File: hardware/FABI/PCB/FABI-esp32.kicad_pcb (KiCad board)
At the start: 2 copper layers, 41 x 73 mm, 93 parts, among them J1 PJ320D, J10 Conn_01x06, J11 PJ320D, J12 Conn_01x08, J13 tp, J14 tp, J15 tp, J16 tp, J17 tp, J2 PJ320D, J3 PJ320D, J4 PJ320D, J5 PJ320D, J6 PJ320D, J7 PJ320D, J8 Conn_01x04, J9 USB_OTG, Q1 BC847, Q2 BSH108, Q3 BC847, Q4 BSH108, Q5 BSH108, Q6 BSH108, SW1 SW_Push, U1 ESP32-WROOM, U3 LPC11U14FBD, U4 TSR 1 (0.5) -2433, Y1 JA-12.000-18-DFE

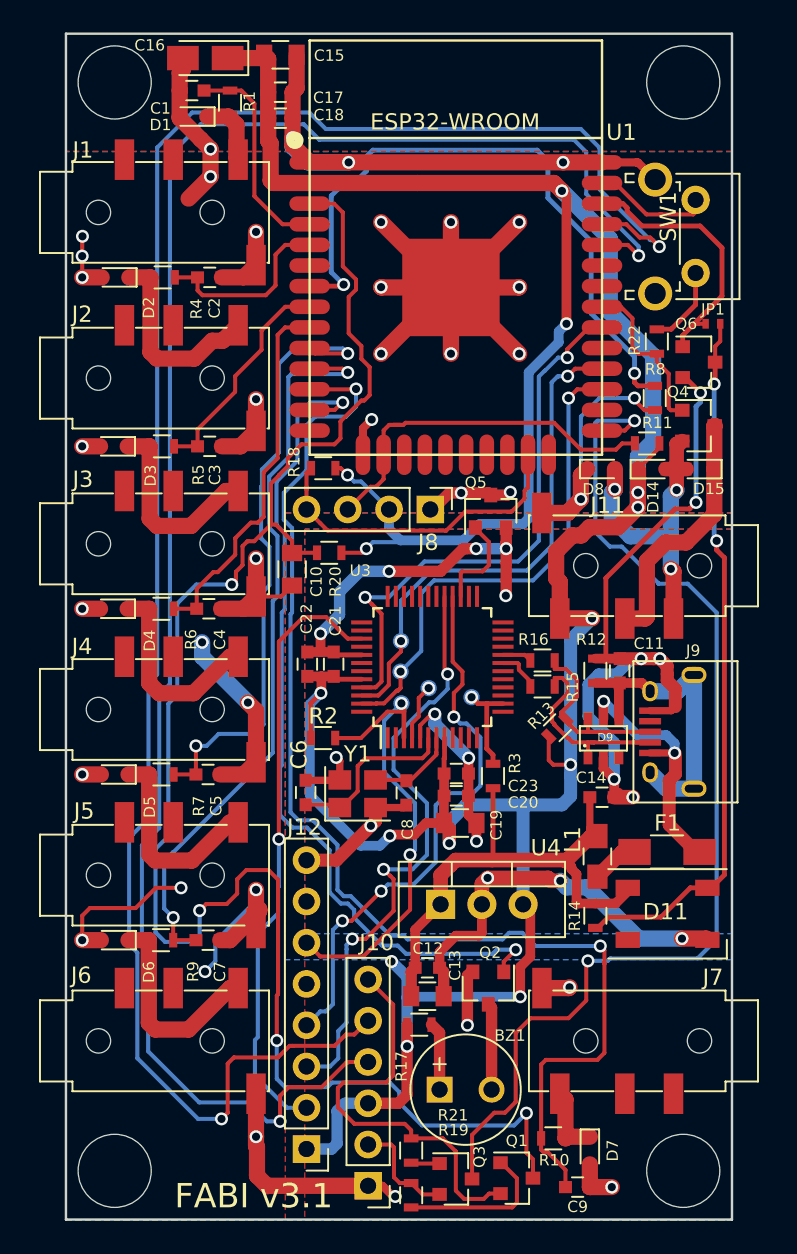
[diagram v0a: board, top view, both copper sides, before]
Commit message: PCB updates: -) Changed TVS diodes to same array as used for USB -) modified part positions to avoid courtyard errors -) Modified SK6812 circuit (use diode to reduce supply voltage of led -> drivable with 3v3 signals)
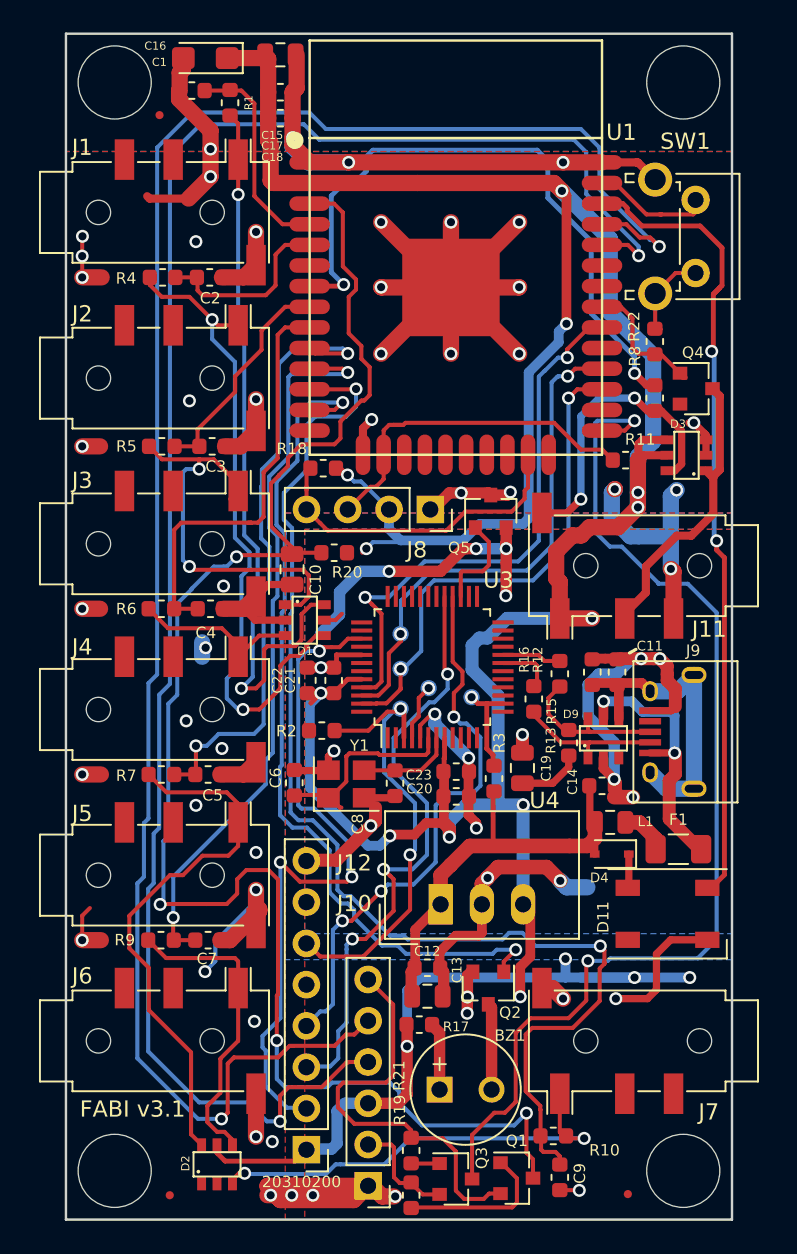
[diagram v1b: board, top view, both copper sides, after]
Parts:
- removed ? (x4): TEST, Mounting_Holes:MountingHole_4.5mm
- removed D14, D15, D8: NNCD5.6C-T1-A, Diodes_SMD:D_0603
- removed D5, D6, D7: PESD3V3C1BSFYL, Diodes_SMD:D_0603
- removed JP1: IO direct, Resistors_SMD:R_0402_NoSilk
- removed Q6: BSH108, TO_SOT_Packages_SMD:SOT-23
- removed R14: 1k, Resistors_SMD:R_0603
- added REF**: Fiducial_0.5mm_Dia_1mm_Outer, Fiducial:Fiducial_0.5mm_Dia_1mm_Outer, F.Cu at (106.4, 171.5)
- added REF**: Fiducial_0.5mm_Dia_1mm_Outer, Fiducial:Fiducial_0.5mm_Dia_1mm_Outer, F.Cu at (134.6, 171.4)
- added REF**: Fiducial_0.5mm_Dia_1mm_Outer, Fiducial:Fiducial_0.5mm_Dia_1mm_Outer, F.Cu at (105.8, 105.0)
- added TP1: TEST, Mount:MountingHole_4.5mm_wo_crtyd, F.Cu at (103.0, 103.0)
- added TP2: TEST, Mount:MountingHole_4.5mm_wo_crtyd, F.Cu at (138.0, 103.0)
- added TP3: TEST, Mount:MountingHole_4.5mm_wo_crtyd, F.Cu at (138.0, 170.0)
- added TP4: TEST, Mount:MountingHole_4.5mm_wo_crtyd, F.Cu at (103.0, 170.0)
- BZ1: footprint Buzzers_Beepers:MagneticBuzzer_Kingstate_KCG0601 -> Buzzer_Beeper:MagneticBuzzer_Kingstate_KCG0601
- C1, C11, C12, C14, C17, C18, C2, C20, C21, C22, C23, C3, C4, C5, C6, C7, C8, C9: footprint Capacitors_SMD:C_0603 -> Capacitor_SMD:C_0603_1608Metric
- C10, C13, C15, C19: footprint Capacitors_SMD:C_0805 -> Capacitor_SMD:C_0805_2012Metric
- C16: value 100uF -> 15uF; footprint Capacitors_Tantalum_SMD:CP_Tantalum_Case-A_EIA-3216-18_Reflow -> Capacitor_Tantalum_SMD:CP_EIA-3216-18_Kemet-A
- D1, D2, D3: value PESD3V3C1BSFYL -> IP4220CZ6,125; footprint Diodes_SMD:D_0603 -> SOT457:SOT457
- D4: value PESD3V3C1BSFYL -> 1N4148WS; footprint Diodes_SMD:D_0603 -> Diode_SMD:D_SOD-323
- F1: footprint Capacitors_SMD:C_1206_HandSoldering -> Capacitor_SMD:C_1206_3216Metric
- J1, J11, J2, J3, J4, J5, J6, J7: footprint Connect:PJ320D_3.5mm_Jack -> Connector_Audio:Jack_3.5mm_PJ320D_Horizontal
- J10: footprint Pin_Headers:Pin_Header_Straight_1x06_Pitch2.54mm -> Connector_PinHeader_2.54mm:PinHeader_1x06_P2.54mm_Vertical
- J12: value Conn_01x08 -> Conn_01x08_Male; footprint Pin_Headers:Pin_Header_Straight_1x08_Pitch2.54mm -> Connector_PinHeader_2.54mm:PinHeader_1x08_P2.54mm_Vertical
- J13, J14, J15, J16, J17: footprint Measurement_Points:Measurement_Point_Round-SMD-Pad_Small -> TestPoint:TestPoint_Pad_D1.0mm
- J8: footprint Pin_Headers:Pin_Header_Straight_1x04_Pitch2.54mm -> Connector_PinSocket_2.54mm:PinSocket_1x04_P2.54mm_Vertical
- L1: footprint Capacitors_SMD:C_0805_HandSoldering -> Inductor_SMD:L_0805_2012Metric
- Q1, Q2, Q3, Q4, Q5: footprint TO_SOT_Packages_SMD:SOT-23 -> Package_TO_SOT_SMD:SOT-23
- R1, R10, R11, R12, R13, R15, R16, R17, R18, R19, R2, R20, R21, R22, R3, R4, R5, R6, R7, R8, R9: footprint Resistors_SMD:R_0603 -> Resistor_SMD:R_0603_1608Metric
- U3: footprint Housings_QFP:LQFP-48_7x7mm_Pitch0.5mm -> Package_QFP:LQFP-48_7x7mm_P0.5mm
- U4: value TSR 1 (0.5) -2433 -> TSR_1-2433; footprint TO_SOT_Packages_THT:TO-220_Vertical -> Converter_DCDC:Converter_DCDC_TRACO_TSR-1_THT
- Y1: footprint Crystals:Crystal_SMD_3225-4pin_3.2x2.5mm -> Crystal:Crystal_SMD_3225-4Pin_3.2x2.5mm
- moved D2 55.0 mm to (109.3, 169.6), turned to 0 degrees
- moved D3 35.3 mm to (138.2, 126.0), turned to 90 degrees
- moved D4 34.2 mm to (133.6, 150.5)
- moved D1 31.7 mm to (114.7, 136.1), turned to 270 degrees
- moved C19 5.12 mm to (128.1, 145.2), turned to 90 degrees
- moved Q4 2.28 mm to (138.8, 121.8)
- moved L1 2.23 mm to (133.5, 148.6), turned to 180 degrees
- moved R11 1.68 mm to (134.4, 126.2)
- moved R16 1.34 mm to (130.4, 139.4), turned to 270 degrees
- moved C9 1.25 mm to (130.4, 170.4), turned to 90 degrees
- moved R13 1.16 mm to (130.9, 143.7), turned to 270 degrees
- moved C21 1.00 mm to (116.5, 139.8)
- moved C22 1.00 mm to (114.9, 139.8)
- moved R15 0.94 mm to (128.8, 140.9), turned to 270 degrees
- moved C8 0.92 mm to (120.3, 146.1)
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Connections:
- net Net-(R15-Pad1) renamed /DD-
- net Net-(R16-Pad1) renamed /DD+
- D11 pad 1: GND -> GNDD
- D11 pad 3: VBUS -> Net-(D11-Pad3)
- D11 pad 4: Net-(D11-Pad4) -> (no net)
- D2 pad 1: Net-(D2-Pad1) -> GNDD
- D4 pad 1: Net-(D4-Pad1) -> Net-(D11-Pad3)
- D4 pad 2: GNDD -> VBUS
- D9 pad 3: Net-(D9-Pad3) -> (no net)
- J1 pad 1: Net-(D1-Pad1) -> Net-(D1-Pad6)
- J1 pad 2: Net-(J1-Pad2) -> GNDD
- J1 pad 3: Net-(J1-Pad3) -> GNDD
- J11 pad 2: Net-(D15-Pad1) -> Net-(D3-Pad1)
- J11 pad 4: Net-(D8-Pad1) -> Net-(D3-Pad6)
- J12 pad 5: Net-(J12-Pad5) -> (no net)
- J12 pad 7: Net-(J12-Pad7) -> (no net)
- J2 pad 1: Net-(D2-Pad1) -> Net-(D1-Pad4)
- J2 pad 2: Net-(J2-Pad2) -> (no net)
- J2 pad 3: Net-(J2-Pad3) -> (no net)
- J3 pad 1: Net-(D3-Pad1) -> Net-(D1-Pad1)
- J3 pad 2: Net-(J3-Pad2) -> (no net)
- J3 pad 3: Net-(J3-Pad3) -> (no net)
- J4 pad 1: Net-(D4-Pad1) -> Net-(D1-Pad3)
- J4 pad 2: Net-(J4-Pad2) -> (no net)
- J4 pad 3: Net-(J4-Pad3) -> (no net)
- J5 pad 1: Net-(D5-Pad1) -> Net-(D2-Pad6)
- J5 pad 2: Net-(J5-Pad2) -> (no net)
- J5 pad 3: Net-(J5-Pad3) -> (no net)
- J6 pad 1: Net-(D6-Pad1) -> Net-(D2-Pad4)
- J6 pad 2: Net-(J6-Pad2) -> (no net)
- J6 pad 3: Net-(J6-Pad3) -> (no net)
- J7 pad 1: Net-(D7-Pad1) -> Net-(D2-Pad3)
- J7 pad 2: Net-(J7-Pad2) -> (no net)
- J7 pad 3: Net-(J7-Pad3) -> (no net)
- J9 pad 4: Net-(J9-Pad4) -> (no net)
- Q4 pad 3: Net-(D15-Pad1) -> Net-(D3-Pad1)
- R1 pad 1: Net-(D1-Pad1) -> Net-(D1-Pad6)
- R10 pad 1: Net-(D7-Pad1) -> Net-(D2-Pad3)
- R4 pad 1: Net-(D2-Pad1) -> Net-(D1-Pad4)
- R5 pad 1: Net-(D3-Pad1) -> Net-(D1-Pad1)
- R6 pad 1: Net-(D4-Pad1) -> Net-(D1-Pad3)
- R7 pad 1: Net-(D5-Pad1) -> Net-(D2-Pad6)
- R8 pad 2: Net-(D8-Pad1) -> Net-(D3-Pad6)
- R9 pad 1: Net-(D6-Pad1) -> Net-(D2-Pad4)
- U1 pad 14: Net-(U1-Pad14) -> (no net)
- U1 pad 17: Net-(U1-Pad17) -> (no net)
- U1 pad 18: Net-(U1-Pad18) -> (no net)
- U1 pad 19: Net-(U1-Pad19) -> (no net)
- U1 pad 20: Net-(U1-Pad20) -> (no net)
- U1 pad 21: Net-(U1-Pad21) -> (no net)
- U1 pad 22: Net-(U1-Pad22) -> (no net)
- U1 pad 24: Net-(U1-Pad24) -> (no net)
- U1 pad 26: Net-(U1-Pad26) -> (no net)
- U1 pad 29: Net-(U1-Pad29) -> (no net)
- U1 pad 32: Net-(U1-Pad32) -> (no net)
- U1 pad 33: Net-(U1-Pad33) -> (no net)
- U1 pad 36: Net-(JP1-Pad1) -> /LED1
- U1 pad 6: Net-(U1-Pad6) -> (no net)
- U3 pad 1: Net-(U3-Pad1) -> (no net)
- U3 pad 10: Net-(U3-Pad10) -> (no net)
- U3 pad 11: Net-(U3-Pad11) -> (no net)
- U3 pad 12: Net-(U3-Pad12) -> (no net)
- U3 pad 13: Net-(U3-Pad13) -> (no net)
- U3 pad 15: Net-(U3-Pad15) -> (no net)
- U3 pad 16: Net-(U3-Pad16) -> (no net)
- U3 pad 17: Net-(U3-Pad17) -> (no net)
- U3 pad 18: Net-(U3-Pad18) -> (no net)
- U3 pad 2: Net-(U3-Pad2) -> (no net)
- U3 pad 21: Net-(U3-Pad21) -> (no net)
- U3 pad 22: Net-(U3-Pad22) -> (no net)
- U3 pad 23: Net-(U3-Pad23) -> (no net)
- U3 pad 24: Net-(U3-Pad24) -> (no net)
- U3 pad 25: Net-(U3-Pad25) -> (no net)
- U3 pad 26: Net-(U3-Pad26) -> (no net)
- U3 pad 30: Net-(U3-Pad30) -> (no net)
- U3 pad 31: Net-(U3-Pad31) -> (no net)
- U3 pad 32: Net-(U3-Pad32) -> (no net)
- U3 pad 33: Net-(U3-Pad33) -> (no net)
- U3 pad 34: Net-(U3-Pad34) -> (no net)
- U3 pad 35: Net-(U3-Pad35) -> (no net)
- U3 pad 36: Net-(U3-Pad36) -> (no net)
- U3 pad 37: Net-(U3-Pad37) -> (no net)
- U3 pad 38: Net-(U3-Pad38) -> (no net)
- U3 pad 40: Net-(U3-Pad40) -> (no net)
- U3 pad 42: Net-(U3-Pad42) -> (no net)
- U3 pad 43: Net-(U3-Pad43) -> (no net)
- U3 pad 48: Net-(U3-Pad48) -> (no net)
- U3 pad 9: Net-(U3-Pad9) -> (no net)
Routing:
- net Net-(D1-Pad6): track 0.00 -> 45.6 mm, vias 0 -> 2
- net Net-(D1-Pad4): track 0.00 -> 40.9 mm, vias 0 -> 2
- net Net-(D2-Pad6): track 0.00 -> 33.8 mm
- net GND: track 115.0 -> 85.5 mm, vias 19 -> 17
- net Net-(D2-Pad3): track 0.00 -> 27.0 mm, vias 0 -> 2
- net +3V3: track 200.3 -> 226.1 mm, vias 14 -> 16
- net Net-(D1-Pad1): track 4.20 -> 25.8 mm, vias 0 -> 2
- net Net-(D3-Pad6): track 0.00 -> 20.2 mm, vias 0 -> 2
- net Net-(D2-Pad4): track 0.00 -> 19.1 mm
- net Net-(JP1-Pad1): track 16.4 -> 0.00 mm
- net Net-(D15-Pad1): track 15.7 -> 0.00 mm
- net Net-(D8-Pad1): track 15.4 -> 0.00 mm, vias 2 -> 0
- net Net-(D6-Pad1): track 13.1 -> 0.00 mm
- net Net-(D5-Pad1): track 12.8 -> 0.00 mm
- net Net-(D4-Pad1): track 12.6 -> 0.00 mm
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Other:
- board text added: "(C) AsTeRICS Foundation, 2018 Benjamin Aigner <office@asterics-foundation.org> FABI v3.1"
- board text added: "20310200"
- board text added: "J13:LPC reset,P0.0 J14:LPC boot mode,P0.1 J15:LPC boot MSD,P0.3 J16:LPC RX,P0.18 J17:LPC TX,P0.19"
- board text added: "RoHS"
- board text removed: "(C) AsTeRICS Foundation, 2018 Benjamin Aigner <office@asterics-foundation.org> FABI v3.0"
- board text removed: "Supported by:"

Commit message: Finalized FABI PCB, added PDFs & finalized BOM
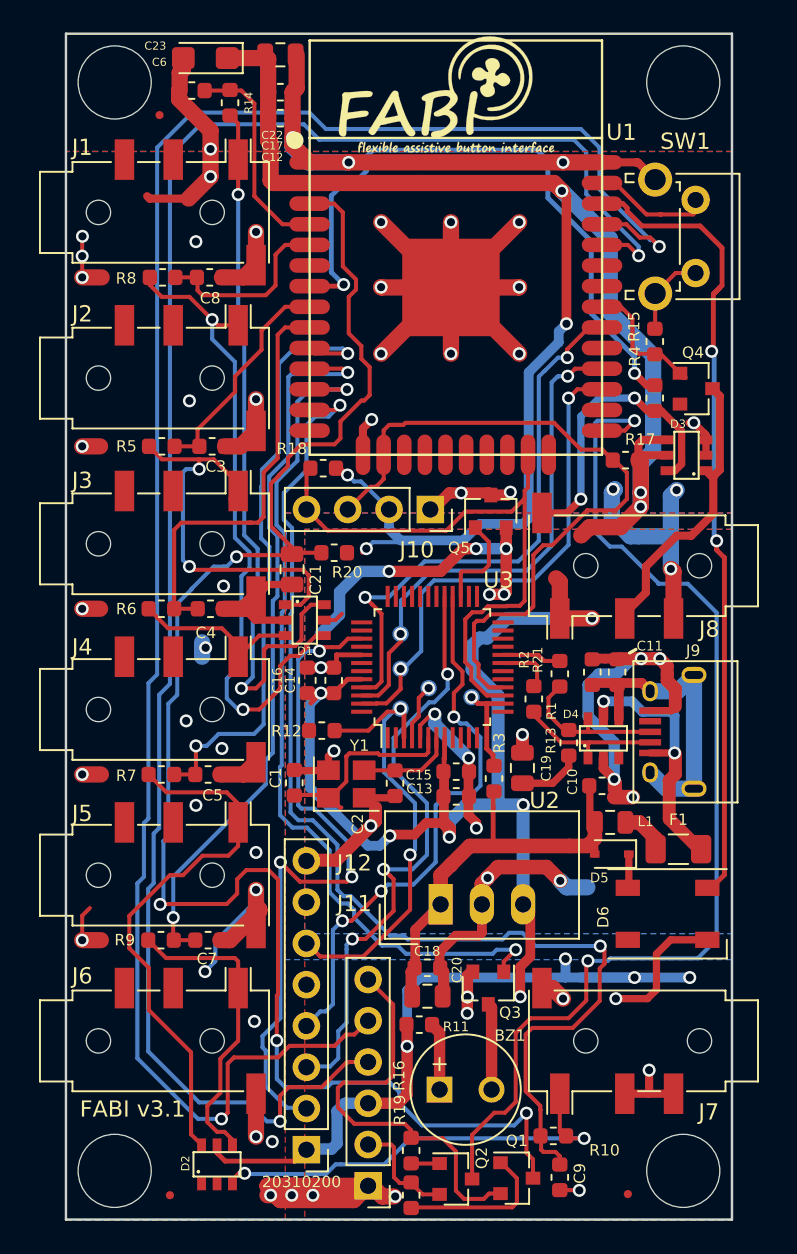
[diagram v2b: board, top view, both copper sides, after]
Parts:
- removed REF** (x3): Fiducial_0.5mm_Dia_1mm_Outer, Fiducial:Fiducial_0.5mm_Dia_1mm_Outer
- added FID1: Fiducial, Fiducial:Fiducial_0.5mm_Dia_1mm_Outer, F.Cu at (105.8, 105.0)
- added FID2: Fiducial, Fiducial:Fiducial_0.5mm_Dia_1mm_Outer, F.Cu at (106.4, 171.5)
- added FID3: Fiducial, Fiducial:Fiducial_0.5mm_Dia_1mm_Outer, F.Cu at (134.6, 171.4)
- added LOGO1: LOGO_CE, Logo:CE, B.Cu at (131.8, 170.2)
- added LOGO2: LOGO_FABI, Logo:fabi_15x8, B.Cu at (126.1, 115.4)
- added LOGO3: LOGO_WEEE, Symbol:WEEE-Logo_4.2x6mm_SilkScreen, B.Cu at (125.6, 169.2)
- added LOGO4: LOGO_FABI, Logo:fabi_15x8, F.Cu at (122.8, 103.7)
- renumbered C6 to C1, C14 to C10, C18 to C12, C20 to C13, C21 to C14, C23 to C15, C22 to C16, C12 to C18, C8 to C2, C13 to C20, C10 to C21, C15 to C22, C16 to C23, C1 to C6, C2 to C8, D9 to D4, D4 to D5, D11 to D6, J8 to J10, J10 to J11, J11 to J8, TP1 to MH1, TP2 to MH2, TP3 to MH3, TP4 to MH4, Q3 to Q2, Q2 to Q3, R15 to R1, R17 to R11, R2 to R12, R1 to R14, R22 to R15, R21 to R16, R11 to R17, R16 to R2, R12 to R21, R8 to R4, R4 to R8, U4 to U2
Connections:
- J2 pad 2: (no net) -> GNDD
- J2 pad 3: (no net) -> GNDD
- J3 pad 2: (no net) -> GNDD
- J3 pad 3: (no net) -> GNDD
- J4 pad 2: (no net) -> GNDD
- J4 pad 3: (no net) -> GNDD
- J5 pad 2: (no net) -> GNDD
- J5 pad 3: (no net) -> GNDD
- J6 pad 2: (no net) -> GNDD
- J6 pad 3: (no net) -> GNDD
- J7 pad 2: (no net) -> GNDD
- J7 pad 3: (no net) -> GNDD
- U1 pad 12: /B_6 -> /BUZZER
- U1 pad 13: /BUZZER -> /B_6
- U3 pad 15: (no net) -> /SCL
- U3 pad 16: (no net) -> /SDA
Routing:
- net /SDA: track 21.7 -> 44.1 mm
- net /SCL: track 20.2 -> 36.9 mm
- net GNDD: track 190.2 -> 194.7 mm, vias 51 -> 52
- net +3V3: track 226.1 -> 222.6 mm
- net /B_6: track 75.0 -> 72.1 mm
- net /BUZZER: track 52.4 -> 53.6 mm
- net GND: track 85.5 -> 86.5 mm, vias 17 -> 18

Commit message: 3D cleanup, should be now ready for production
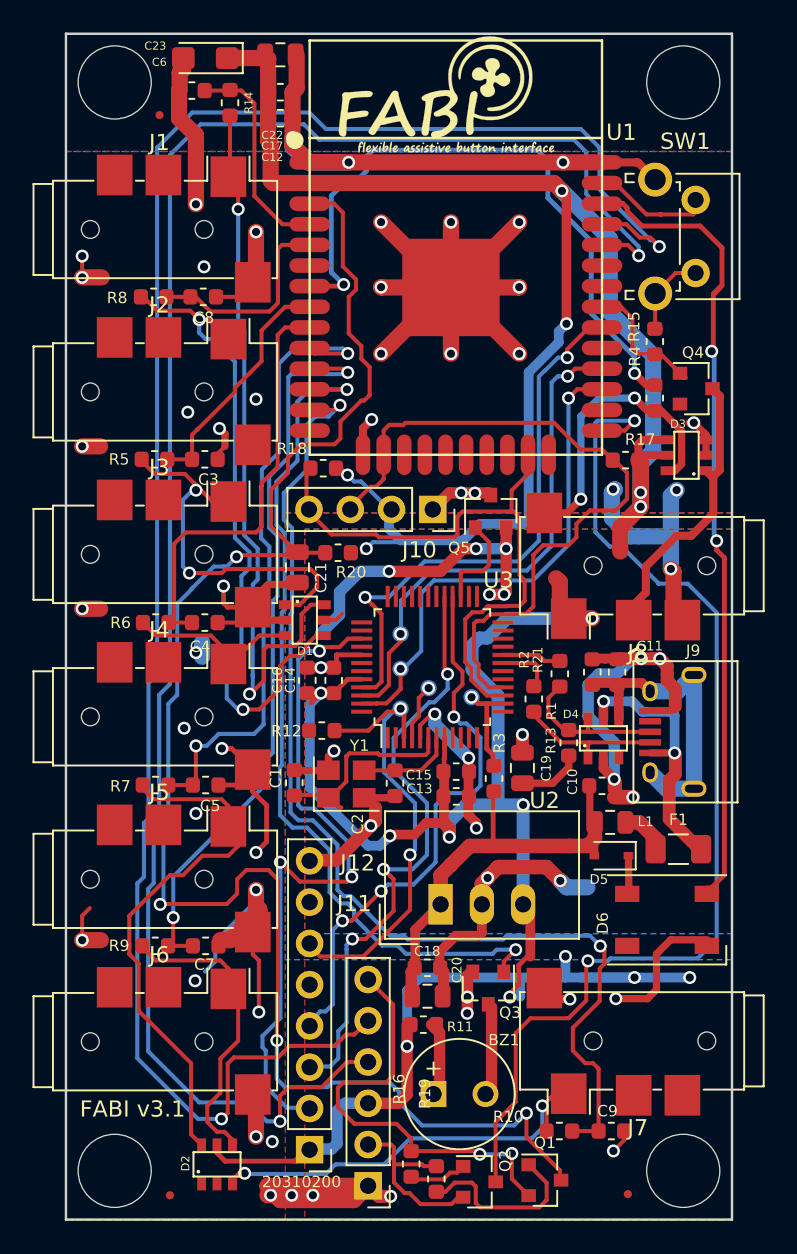
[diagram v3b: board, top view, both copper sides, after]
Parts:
- J1, J2, J3, J4, J5, J6, J7, J8: value PJ320D -> SJ2-3574A; footprint Connector_Audio:Jack_3.5mm_PJ320D_Horizontal -> JackPlug:Jack_3.5mm_SJ2-357X
- moved J1 7.65 mm to (99.2, 112.0)
- moved J2 7.62 mm to (99.2, 122.0)
- moved J3 7.60 mm to (99.2, 132.1)
- moved J4 7.59 mm to (99.2, 142.1)
- moved J5 7.58 mm to (99.2, 152.1)
- moved J6 7.58 mm to (99.2, 162.1)
- moved J7 7.53 mm to (141.8, 162.0)
- moved J8 7.53 mm to (141.8, 132.8)
- moved C9 4.27 mm to (133.6, 167.6), turned to 180 degrees
- moved R19 1.84 mm to (122.8, 170.5)
- moved Q1 1.73 mm to (129.5, 170.6)
- moved Q2 1.46 mm to (125.5, 170.7)
- moved R8 1.32 mm to (105.4, 116.2)
- moved C8 1.26 mm to (108.5, 116.2)
- moved C4 0.92 mm to (108.5, 136.2)
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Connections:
- J1 pad 1: Net-(D1-Pad6) -> GNDD
- J1 pad 2: GNDD -> Net-(D1-Pad6)
- J1 pad 3: GNDD -> (no net)
- J1 pad 4: GNDD -> (no net)
- J2 pad 1: Net-(D1-Pad4) -> GNDD
- J2 pad 2: GNDD -> Net-(D1-Pad4)
- J2 pad 3: GNDD -> (no net)
- J2 pad 4: GNDD -> (no net)
- J3 pad 1: Net-(D1-Pad1) -> GNDD
- J3 pad 2: GNDD -> Net-(D1-Pad1)
- J3 pad 3: GNDD -> (no net)
- J3 pad 4: GNDD -> (no net)
- J4 pad 1: Net-(D1-Pad3) -> GNDD
- J4 pad 2: GNDD -> Net-(D1-Pad3)
- J4 pad 3: GNDD -> (no net)
- J4 pad 4: GNDD -> (no net)
- J5 pad 1: Net-(D2-Pad6) -> GNDD
- J5 pad 2: GNDD -> Net-(D2-Pad6)
- J5 pad 3: GNDD -> (no net)
- J5 pad 4: GNDD -> (no net)
- J6 pad 1: Net-(D2-Pad4) -> GNDD
- J6 pad 2: GNDD -> Net-(D2-Pad4)
- J6 pad 3: GNDD -> (no net)
- J6 pad 4: GNDD -> (no net)
- J7 pad 1: Net-(D2-Pad3) -> GNDD
- J7 pad 2: GNDD -> Net-(D2-Pad3)
- J7 pad 3: GNDD -> (no net)
- J7 pad 4: GNDD -> (no net)
- J8 pad 1: +3V3 -> Net-(D3-Pad6)
- J8 pad 2: Net-(D3-Pad1) -> +3V3
- J8 pad 3: GNDD -> Net-(D3-Pad1)
- J8 pad 4: Net-(D3-Pad6) -> GNDD
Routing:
- net GNDD: track 194.7 -> 202.6 mm, vias 52 -> 49
- net Net-(J11-Pad2): track 6.75 -> 11.5 mm
- net /B_6: track 72.1 -> 68.5 mm
- net Net-(D1-Pad6): track 45.6 -> 48.7 mm
- net Net-(D1-Pad1): track 25.8 -> 23.8 mm
- net Net-(Q2-Pad1): track 1.77 -> 3.60 mm
- net /SCL: track 36.9 -> 38.7 mm
- net Net-(Q1-Pad1): track 9.54 -> 11.1 mm
- net Net-(J11-Pad6): track 25.7 -> 27.1 mm, vias 0 -> 2
- net Net-(D2-Pad3): track 27.0 -> 25.6 mm
- net /E_RESET: track 100.6 -> 101.8 mm
- net Net-(D1-Pad4): track 40.9 -> 42.1 mm
- net /B_1: track 11.6 -> 12.8 mm
- net /B_2: track 13.8 -> 14.8 mm
- net /E_P0: track 67.7 -> 66.9 mm
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
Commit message: Changed USB chipset to LPC11U__2__4 (from LPC11U14): This introduces the possibility to use the USB-MSD bootloader for software updates. Otherwise we would need either a serial adapter, a custom bootloader or a programming software within the ESP32 (and more nets between these two chips).
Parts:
- U3: value LPC11U14FBD -> LPC11U24FBD
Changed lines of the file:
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@@
       (effects (font (size 1 1) (thickness 0.15)))
     )
-    (fp_text value LPC11U14FBD (at 0 6 90) (layer F.Fab)
+    (fp_text value LPC11U24FBD (at 0 6 90) (layer F.Fab)
       (effects (font (size 1 1) (thickness 0.15)))
     )
